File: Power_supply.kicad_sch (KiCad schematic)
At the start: 43 parts, among them IC1 TPS61087DRCR, Q1 DMP2045U, Q3 BC847-QR, U1 LD1117S50, U2 MIC2288, U6 LD1117S33

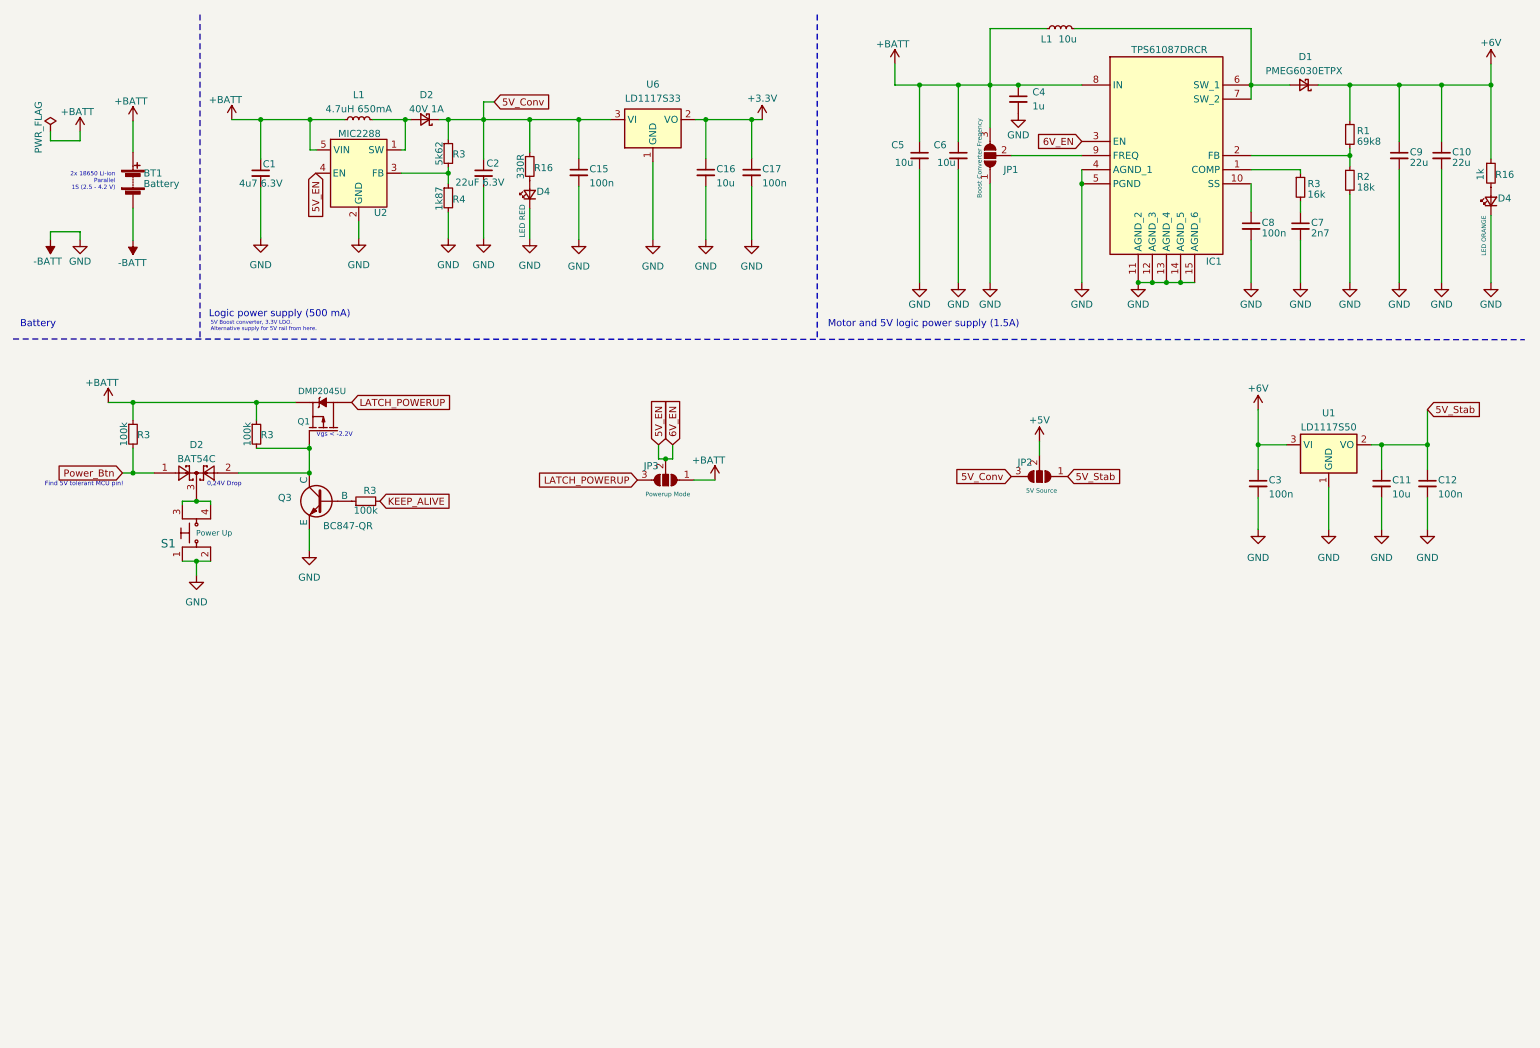
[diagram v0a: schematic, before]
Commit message: schematic completed
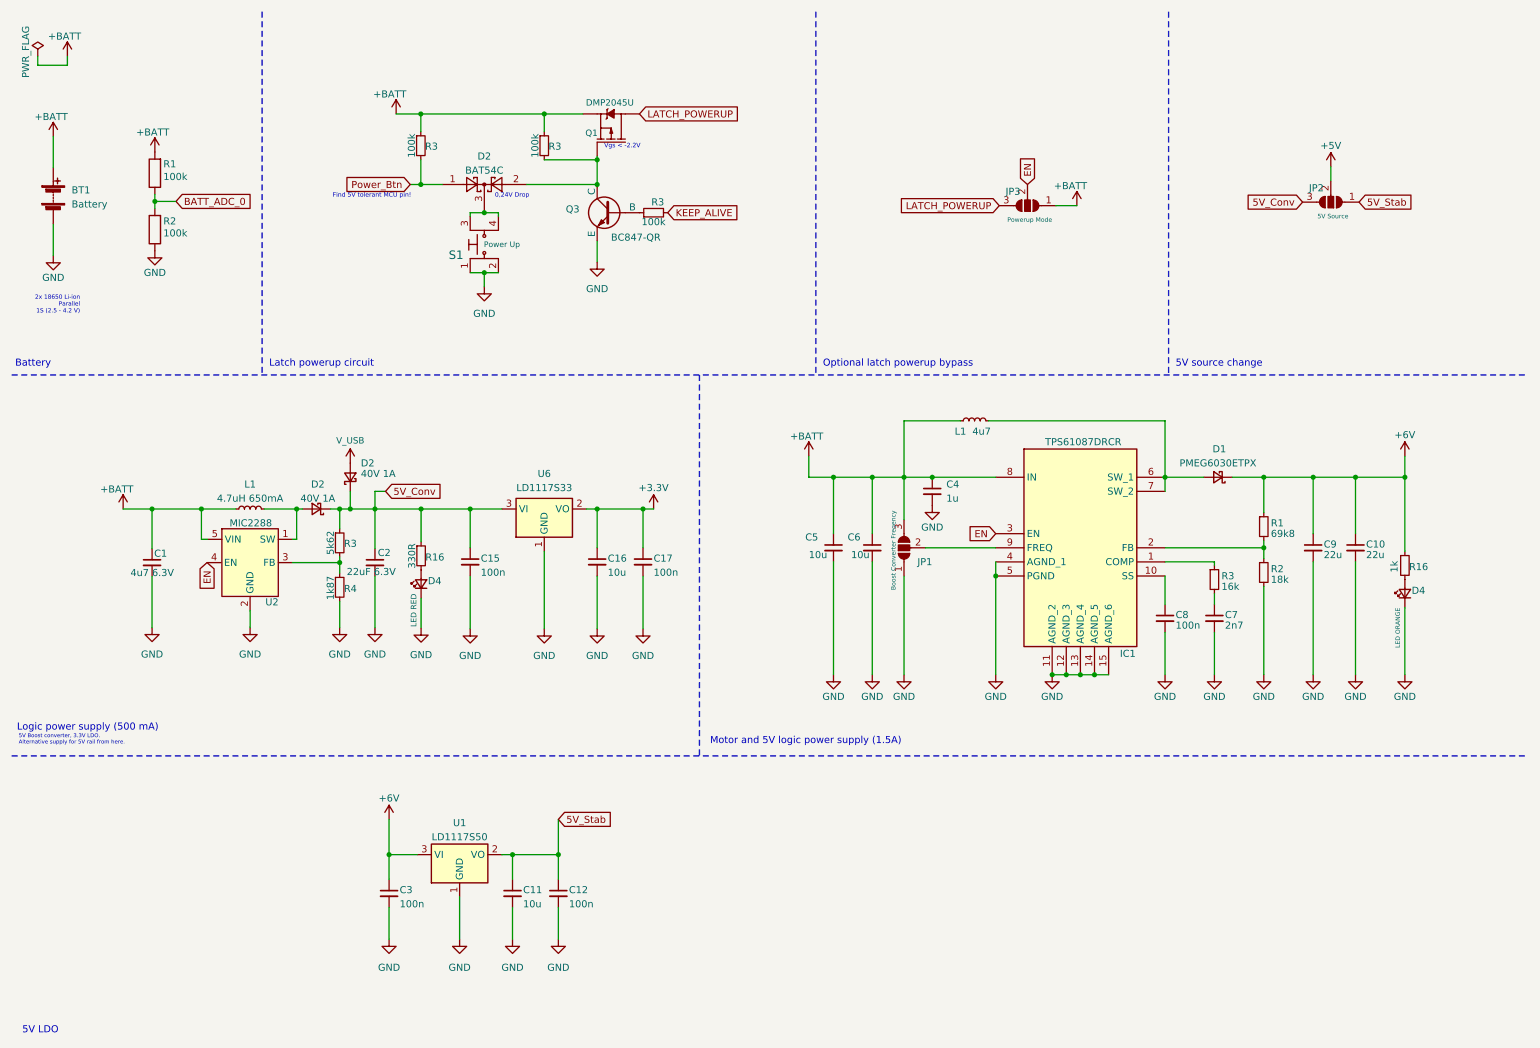
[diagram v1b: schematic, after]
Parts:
- added D2: 40V 1A, Diode_SMD:D_SOD-123, symbol Device:D_Schottky_Small
- added R1, R2: 100k, Resistor_SMD:R_0603_1608Metric, symbol Device:R
- C10, C9: footprint (none) -> Capacitor_SMD:C_0805_2012Metric
- C11, C12, C15, C16, C17, C3, C4, C5, C6, C7, C8: footprint (none) -> Capacitor_SMD:C_0603_1608Metric
- C2: footprint Capacitor_SMD:C_0603_1608Metric -> Capacitor_SMD:C_0805_2012Metric
- D1: footprint (none) -> Diode_SMD:D_SOD-128
- IC1: footprint TPS61087DRCR -> TPS61087DRCR:TPS61087DRCR
- JP1, JP2: footprint (none) -> Jumper:SolderJumper-3_P1.3mm_Open_Pad1.0x1.5mm
- JP3: footprint (none) -> Connector_PinHeader_2.54mm:PinHeader_1x03_P2.54mm_Vertical
- L1: value 10u -> 4u7; footprint (none) -> Inductor_SMD:L_Neosid_SM-PIC0602H
- Q3: footprint (none) -> Package_TO_SOT_SMD:SOT-23
- R1, R2, R3: footprint (none) -> Resistor_SMD:R_0603_1608Metric
- S1: footprint Button_Switch_SMD:SW_MEC_5GSH9 -> TL3305CF160QG:TL3305AF160QG
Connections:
- net +BATT: now also R1.2
- net 5V_Conv: now also D2.1 (K)
- net -BATT renamed GND
- net GND: now also R2.1
- net 5V_EN renamed EN
- new net BATT_ADC_0: R1.1, R2.2
- new net V_USB: D2.2 (A)
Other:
- note added: "5V LDO"
- note added: "5V source change"
- note added: "Latch powerup circuit"
- note added: "Optional latch powerup bypass"
- moved on the sheet: C1, C10, C11, C12, C15, C16, C17, C2, C3, C4, C5, C6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

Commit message: done boost converter layout
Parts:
- BT1: footprint TerminalBlock_Phoenix:TerminalBlock_Phoenix_MKDS-1,5-2-5.08_1x02_P5.08mm_Horizontal -> TerminalBlock_Phoenix:TerminalBlock_Phoenix_PT-1,5-2-3.5-H_1x02_P3.50mm_Horizontal
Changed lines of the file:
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@@
       (effects (font (size 1.27 1.27)) (justify left))
     )
-    (property "Footprint" "TerminalBlock_Phoenix:TerminalBlock_Phoenix_MKDS-1,5-2-5.08_1x02_P5.08mm_Horizontal" (at 19.558 43.688 90)
+    (property "Footprint" "TerminalBlock_Phoenix:TerminalBlock_Phoenix_PT-1,5-2-3.5-H_1x02_P3.50mm_Horizontal" (at 19.558 43.688 90)
       (effects (font (size 1.27 1.27)) hide)
     )

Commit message: working on pcb
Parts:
- removed S1: Power Up, TL3305CF160QG:TL3305AF160QG, symbol dk_Tactile-Switches:1825910-6
- added S5: POWER UP, digikey-footprints:Switch_Tactile_SMD_6x6mm_PTS645, symbol dk_Tactile-Switches:PTS645SM43SMTR92_LFS
- D4: footprint LED_SMD:LED_0805_2012Metric -> LED_SMD:LED_0603_1608Metric
- JP3: footprint Connector_PinHeader_2.54mm:PinHeader_1x03_P2.54mm_Vertical -> Jumper:SolderJumper-3_P1.3mm_Open_Pad1.0x1.5mm
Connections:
- net GND: now also S5.1, S5.2
- net at D2.3: now also S5.3, S5.4

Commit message: more layout added
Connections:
- net at D2.3, S5.4: no longer S5.3
- no-connect marks 0 -> 1
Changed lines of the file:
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@@
   (junction (at 246.38 95.885) (diameter 0) (color 0 0 0 0)
   )
-  (junction (at 97.155 48.26) (diameter 0) (color 0 0 0 0)
-  )
   (junction (at 172.72 95.885) (diameter 0) (color 0 0 0 0)
   )
@@
   (junction (at 85.7758 101.6) (diameter 0) (color 0 0 0 0)
   )
+  (no_connect (at 94.615 48.895))
   (wire (pts (xy 249.555 40.005) (xy 249.555 42.545))
     (stroke (width 0) (type default))
@@
     (stroke (width 0) (type default))
   )
-  (wire (pts (xy 97.155 48.26) (xy 94.615 48.26))
-    (stroke (width 0) (type default))
-  )
   (wire (pts (xy 125.73 101.6) (xy 127.635 101.6))
     (stroke (width 0) (type default))
@@
     (stroke (width 0) (type default))
   )
-  (wire (pts (xy 94.615 48.26) (xy 94.615 48.895))
-    (stroke (width 0) (type default))
-  )

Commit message: layout finalising
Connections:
- net +3.3V: now also R16.1
- net 5V_Conv: no longer R16.1
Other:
- moved on the sheet: D4, R16
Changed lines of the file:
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@@
   (junction (at 107.95 30.48) (diameter 0) (color 0 0 0 0)
   )
+  (junction (at 121.5033 101.6) (diameter 0) (color 0 0 0 0)
+  )
   (junction (at 37.338 101.6) (diameter 0) (color 0 0 0 0)
   )
@@
   )
   (junction (at 189.23 113.665) (diameter 0) (color 0 0 0 0)
-  )
-  (junction (at 85.7758 101.6) (diameter 0) (color 0 0 0 0)
   )
   (no_connect (at 94.615 48.895))
@@
     (stroke (width 0) (type default))
   )
+  (wire (pts (xy 121.5033 101.6) (xy 125.73 101.6))
+    (stroke (width 0) (type default))
+  )
   (wire (pts (xy 77.47 113.792) (xy 77.47 122.936))
     (stroke (width 0) (type default))
@@
   )
   (wire (pts (xy 189.23 111.125) (xy 189.23 113.665))
-    (stroke (width 0) (type default))
-  )
-  (wire (pts (xy 85.7758 101.6) (xy 94.615 101.6))
     (stroke (width 0) (type default))
   )
@@
     (stroke (width 0) (type default))
   )
-  (wire (pts (xy 85.7758 101.6) (xy 85.7758 107.4928))
-    (stroke (width 0) (type default))
-  )
   (wire (pts (xy 97.155 59.055) (xy 94.615 59.055))
     (stroke (width 0) (type default))
@@
     (stroke (width 0) (type default))
   )
-  (wire (pts (xy 77.47 101.6) (xy 85.7758 101.6))
-    (stroke (width 0) (type default))
-  )
-  (wire (pts (xy 117.475 101.6) (xy 125.73 101.6))
+  (wire (pts (xy 77.47 101.6) (xy 94.615 101.6))
+    (stroke (width 0) (type default))
+  )
+  (wire (pts (xy 117.475 101.6) (xy 121.5033 101.6))
     (stroke (width 0) (type default))
   )
@@
     (stroke (width 0) (type default))
   )
+  (wire (pts (xy 121.5033 88.9) (xy 121.5033 101.6))
+    (stroke (width 0) (type default))
+  )
   (wire (pts (xy 237.49 95.885) (xy 237.49 102.235))
     (stroke (width 0) (type default))
@@
     (stroke (width 0) (type default))
   )
+  (wire (pts (xy 113.665 88.9) (xy 121.5033 88.9))
+    (stroke (width 0) (type default))
+  )
   (wire (pts (xy 85.725 30.48) (xy 85.725 33.655))
     (stroke (width 0) (type default))
@@
     (stroke (width 0) (type default))
   )
-  (wire (pts (xy 85.7758 117.6528) (xy 85.7758 123.0376))
+  (wire (pts (xy 103.505 88.9) (xy 98.1202 88.9))
     (stroke (width 0) (type default))
   )
@@
     )
   )
-  (symbol (lib_id "Device:R_Small") (at 85.7758 110.0328 0) (unit 1)
-    (in_bom yes) (on_board yes) (dnp no)
-    (property "Reference" "R16" (at 86.5378 110.2868 0)
-      (effects (font (size 1.27 1.27)) (justify left))
-    )
-    (property "Value" "330R" (at 84.1248 112.3188 90)
-      (effects (font (size 1.27 1.27)) (justify left))
-    )
-    (property "Footprint" "Resistor_SMD:R_0603_1608Metric" (at 85.7758 110.0328 0)
-      (effects (font (size 1.27 1.27)) hide)
-    )
-    (property "Datasheet" "~" (at 85.7758 110.0328 0)
+  (symbol (lib_id "Device:R_Small") (at 111.125 88.9 270) (unit 1)
+    (in_bom yes) (on_board yes) (dnp no)
+    (property "Reference" "R16" (at 110.871 89.662 0)
+      (effects (font (size 1.27 1.27)) (justify left))
+    )
+    (property "Value" "330R" (at 108.839 87.249 90)
+      (effects (font (size 1.27 1.27)) (justify left))
+    )
+    (property "Footprint" "Resistor_SMD:R_0603_1608Metric" (at 111.125 88.9 0)
+      (effects (font (size 1.27 1.27)) hide)
+    )
+    (property "Datasheet" "~" (at 111.125 88.9 0)
       (effects (font (size 1.27 1.27)) hide)
     )
@@
     )
   )
-  (symbol (lib_id "power:GND") (at 85.7758 123.0376 0) (unit 1)
+  (symbol (lib_id "power:GND") (at 98.1202 88.9 270) (unit 1)
     (in_bom yes) (on_board yes) (dnp no) (fields_autoplaced)
-    (property "Reference" "#PWR077" (at 85.7758 129.3876 0)
-      (effects (font (size 1.27 1.27)) hide)
-    )
-    (property "Value" "GND" (at 85.7758 127.8636 0)
-      (effects (font (size 1.27 1.27)))
-    )
-    (property "Footprint" "" (at 85.7758 123.0376 0)
-      (effects (font (size 1.27 1.27)) hide)
-    )
-    (property "Datasheet" "" (at 85.7758 123.0376 0)
+    (property "Reference" "#PWR077" (at 91.7702 88.9 0)
+      (effects (font (size 1.27 1.27)) hide)
+    )
+    (property "Value" "GND" (at 93.2942 88.9 0)
+      (effects (font (size 1.27 1.27)))
+    )
+    (property "Footprint" "" (at 98.1202 88.9 0)
+      (effects (font (size 1.27 1.27)) hide)
+    )
+    (property "Datasheet" "" (at 98.1202 88.9 0)
       (effects (font (size 1.27 1.27)) hide)
     )
@@
     )
   )
-  (symbol (lib_id "Device:LED_Small") (at 85.7758 115.1128 90) (unit 1)
-    (in_bom yes) (on_board yes) (dnp no)
-    (property "Reference" "D4" (at 86.995 114.554 90)
+  (symbol (lib_id "Device:LED_Small") (at 106.045 88.9 0) (unit 1)
+    (in_bom yes) (on_board yes) (dnp no)
+    (property "Reference" "D4" (at 106.6038 90.1192 90)
       (effects (font (size 1.27 1.27)) (justify right))
     )
-    (property "Value" "LED RED" (at 84.455 116.84 0)
+    (property "Value" "LED RED" (at 104.3178 87.5792 0)
       (effects (font (size 1 1)) (justify right))
     )
-    (property "Footprint" "LED_SMD:LED_0603_1608Metric" (at 85.7758 115.1128 90)
-      (effects (font (size 1.27 1.27)) hide)
-    )
-    (property "Datasheet" "~" (at 85.7758 115.1128 90)
-      (effects (font (size 1.27 1.27)) hide)
-    )
+    (property "Footprint" "LED_SMD:LED_0603_1608Metric" (at 106.045 88.9 90)
+      (effects (font (size 1.27 1.27)) hide)
+    )
+    (property "Datasheet" "~" (at 106.045 88.9 90)
+      (effects (font (size 1.27 1.27)) hide)
+    )

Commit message: Completed PCB v1.0
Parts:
- JP1, JP2, JP3: footprint Jumper:SolderJumper-3_P1.3mm_Open_Pad1.0x1.5mm -> Jumper:SolderJumper-3_P1.3mm_Open_RoundedPad1.0x1.5mm
- S5: footprint digikey-footprints:Switch_Tactile_SMD_6x6mm_PTS645 -> digikey-footprints:Switch_Tactile_SMD_6x6mm
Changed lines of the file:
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@@
       (effects (font (size 0.8 0.8)) (justify left))
     )
-    (property "Footprint" "Jumper:SolderJumper-3_P1.3mm_Open_Pad1.0x1.5mm" (at 194.945 46.99 0)
+    (property "Footprint" "Jumper:SolderJumper-3_P1.3mm_Open_RoundedPad1.0x1.5mm" (at 194.945 46.99 0)
       (effects (font (size 1.27 1.27)) hide)
     )
@@
       (effects (font (size 0.8 0.8)) (justify left))
     )
-    (property "Footprint" "Jumper:SolderJumper-3_P1.3mm_Open_Pad1.0x1.5mm" (at 249.555 46.355 0)
+    (property "Footprint" "Jumper:SolderJumper-3_P1.3mm_Open_RoundedPad1.0x1.5mm" (at 249.555 46.355 0)
       (effects (font (size 1.27 1.27)) hide)
     )
@@
       (effects (font (size 1 1)) (justify right))
     )
-    (property "Footprint" "digikey-footprints:Switch_Tactile_SMD_6x6mm_PTS645" (at 92.075 48.895 0)
+    (property "Footprint" "digikey-footprints:Switch_Tactile_SMD_6x6mm" (at 92.075 48.895 0)
       (effects (font (size 1.524 1.524)) (justify left) hide)
     )
@@
       (effects (font (size 0.8 0.8)) (justify left))
     )
-    (property "Footprint" "Jumper:SolderJumper-3_P1.3mm_Open_Pad1.0x1.5mm" (at 172.72 108.585 0)
-      (effects (font (size 1.27 1.27)) hide)
-    )
+    (property "Footprint" "Jumper:SolderJumper-3_P1.3mm_Open_RoundedPad1.0x1.5mm" (at 172.72 108.585 0)
+      (effects (font (size 1.27 1.27)) hide)
+    )
